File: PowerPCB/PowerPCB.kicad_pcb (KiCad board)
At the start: 2 copper layers, 140 x 70 mm, 60 parts, among them J1 Conn_01x03_Male, J2 Conn_01x10_Male, J3 Conn_01x07_Male, K1 1721081-5, K2 1721081-5, K3 1721081-5, Q1 Q_PMOS_DGS, U1 NCP1117-5.0_SOT223, U2 NCP1117-3.3_SOT223, U3 MCP2562-E-P, U4 MCP2562-E-P, U5 STM32F413ZHTx

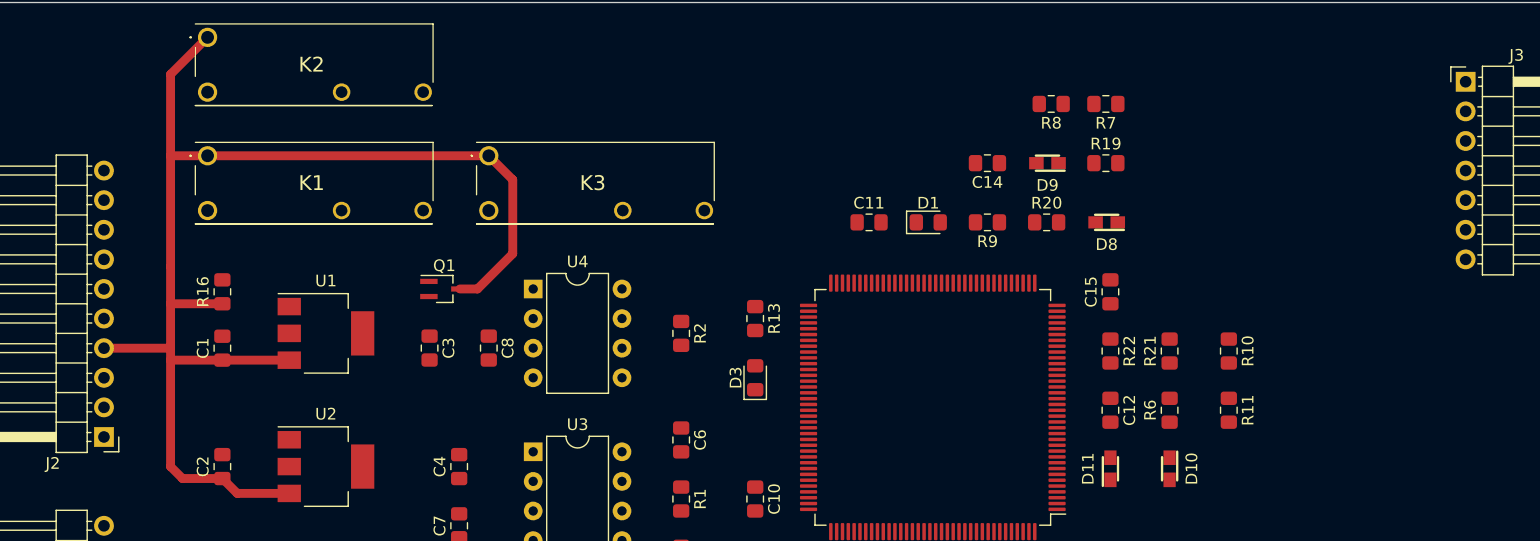
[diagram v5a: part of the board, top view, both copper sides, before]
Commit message: Routed most of Fan circuitry
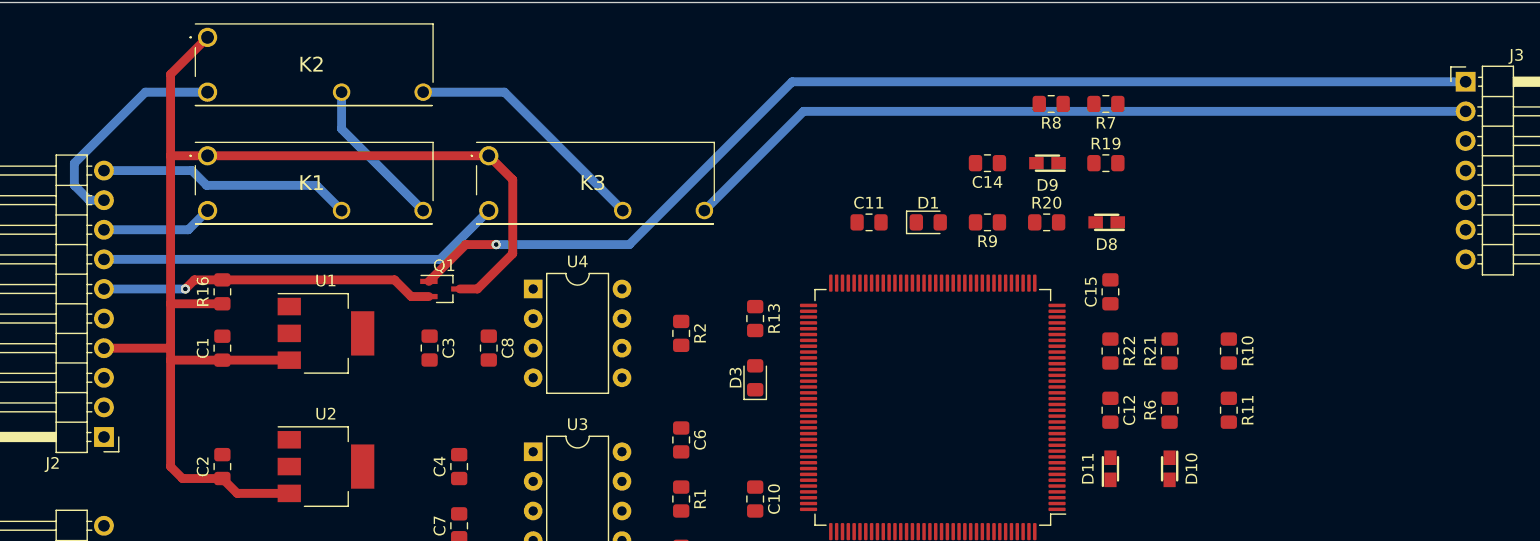
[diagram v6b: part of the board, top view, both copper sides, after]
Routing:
- net /Fan/Fan+: track 0.00 -> 96.1 mm, vias 0 -> 1
- net /Fan/Fan-: track 0.00 -> 68.8 mm
- net /Fan/FanCtrl: track 0.00 -> 34.8 mm
- net /Fan/FanPWM: track 0.00 -> 28.8 mm, vias 0 -> 1
- net Net-(J2-Pad10): track 0.00 -> 21.8 mm
- net GND: track 0.00 -> 21.3 mm
- net Net-(J2-Pad9): track 0.00 -> 18.9 mm
- net Net-(K1-Pad4): track 0.00 -> 13.1 mm
- net Net-(J2-Pad8): track 0.00 -> 9.57 mm
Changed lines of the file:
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@@
     (thickness 1.6)
     (drawings 4)
-    (tracks 21)
+    (tracks 49)
     (zones 0)
     (modules 60)
@@
   (gr_line (start 43 114) (end 183 114) (layer Edge.Cuts) (width 0.05))
   (gr_line (start 43 44) (end 43 114) (layer Edge.Cuts) (width 0.05))
+  (segment (start 88.97 51.69) (end 82 51.69) (width 0.762) (layer B.Cu) (net 1))
+  (segment (start 99.13 61.85) (end 88.97 51.69) (width 0.762) (layer B.Cu) (net 1))
   (segment (start 70.505 74.685) (end 70.51 74.69) (width 0.762) (layer F.Cu) (net 2))
   (segment (start 64.77 74.685) (end 70.505 74.685) (width 0.762) (layer F.Cu) (net 2))
@@
   (segment (start 60.325 50.165) (end 63.5 46.99) (width 0.762) (layer F.Cu) (net 2))
   (segment (start 63.5 57.15) (end 60.325 57.15) (width 0.762) (layer F.Cu) (net 2))
-  (segment (start 60.325 66.675) (end 60.325 57.15) (width 0.762) (layer F.Cu) (net 2))
-  (segment (start 60.325 57.15) (end 60.325 50.165) (width 0.762) (layer F.Cu) (net 2))
   (segment (start 60.325 69.85) (end 64.77 69.85) (width 0.762) (layer F.Cu) (net 2))
-  (segment (start 60.325 69.85) (end 60.325 66.675) (width 0.762) (layer F.Cu) (net 2))
   (segment (start 61.35 84.845) (end 64.77 84.845) (width 0.762) (layer F.Cu) (net 2))
   (segment (start 60.325 83.82) (end 61.35 84.845) (width 0.762) (layer F.Cu) (net 2))
   (segment (start 54.61 73.66) (end 60.325 73.66) (width 0.762) (layer F.Cu) (net 2))
-  (segment (start 60.325 69.85) (end 60.325 73.66) (width 0.762) (layer F.Cu) (net 2))
-  (segment (start 60.325 73.66) (end 60.325 83.82) (width 0.762) (layer F.Cu) (net 2))
   (segment (start 64.77 74.685) (end 60.325 74.685) (width 0.762) (layer F.Cu) (net 2))
   (segment (start 63.5 57.15) (end 87.63 57.15) (width 0.762) (layer F.Cu) (net 2))
@@
   (segment (start 89.686 59.206) (end 87.63 57.15) (width 0.762) (layer F.Cu) (net 2))
   (segment (start 89.686 65.556) (end 89.686 59.206) (width 0.762) (layer F.Cu) (net 2))
+  (segment (start 60.325 83.82) (end 60.325 50.165) (width 0.762) (layer F.Cu) (net 2))
+  (segment (start 61.85 63.5) (end 63.5 61.85) (width 0.762) (layer B.Cu) (net 7))
+  (segment (start 54.61 63.5) (end 61.85 63.5) (width 0.762) (layer B.Cu) (net 7))
+  (segment (start 83.44 66.04) (end 87.63 61.85) (width 0.762) (layer B.Cu) (net 8))
+  (segment (start 54.61 66.04) (end 83.44 66.04) (width 0.762) (layer B.Cu) (net 8))
+  (segment (start 54.61 68.58) (end 61.595 68.58) (width 0.762) (layer B.Cu) (net 9))
+  (via (at 61.595 68.58) (size 0.8) (drill 0.4) (layers F.Cu B.Cu) (net 9))
+  (segment (start 64.77 67.8) (end 62.375 67.8) (width 0.762) (layer F.Cu) (net 9))
+  (segment (start 62.375 67.8) (end 61.595 68.58) (width 0.762) (layer F.Cu) (net 9))
+  (segment (start 80.978 69.23) (end 82.49 69.23) (width 0.762) (layer F.Cu) (net 9))
+  (segment (start 79.548 67.8) (end 80.978 69.23) (width 0.762) (layer F.Cu) (net 9))
+  (segment (start 64.77 67.8) (end 79.548 67.8) (width 0.762) (layer F.Cu) (net 9))
+  (segment (start 114.64 53.34) (end 171.45 53.34) (width 0.762) (layer B.Cu) (net 10))
+  (segment (start 106.13 61.85) (end 114.64 53.34) (width 0.762) (layer B.Cu) (net 10))
+  (via (at 88.265 64.77) (size 0.8) (drill 0.4) (layers F.Cu B.Cu) (net 11))
+  (segment (start 82.49 67.93) (end 85.65 64.77) (width 0.762) (layer F.Cu) (net 11))
+  (segment (start 85.65 64.77) (end 88.265 64.77) (width 0.762) (layer F.Cu) (net 11))
+  (segment (start 88.265 64.77) (end 99.695 64.77) (width 0.762) (layer B.Cu) (net 11))
+  (segment (start 113.665 50.8) (end 171.45 50.8) (width 0.762) (layer B.Cu) (net 11))
+  (segment (start 99.695 64.77) (end 113.665 50.8) (width 0.762) (layer B.Cu) (net 11))
+  (segment (start 75 61.85) (end 72.84 59.69) (width 0.762) (layer B.Cu) (net 16))
+  (segment (start 63.420882 59.69) (end 62.150882 58.42) (width 0.762) (layer B.Cu) (net 16))
+  (segment (start 72.84 59.69) (end 63.420882 59.69) (width 0.762) (layer B.Cu) (net 16))
+  (segment (start 54.61 58.42) (end 62.150882 58.42) (width 0.762) (layer B.Cu) (net 16))
+  (segment (start 58.165 51.69) (end 63.5 51.69) (width 0.762) (layer B.Cu) (net 17))
+  (segment (start 52.07 59.69) (end 52.07 57.785) (width 0.762) (layer B.Cu) (net 17))
+  (segment (start 54.61 60.96) (end 53.34 60.96) (width 0.762) (layer B.Cu) (net 17))
+  (segment (start 52.07 57.785) (end 58.165 51.69) (width 0.762) (layer B.Cu) (net 17))
+  (segment (start 53.34 60.96) (end 52.07 59.69) (width 0.762) (layer B.Cu) (net 17))
+  (segment (start 75 54.85) (end 82 61.85) (width 0.762) (layer B.Cu) (net 20))
+  (segment (start 75 51.69) (end 75 54.85) (width 0.762) (layer B.Cu) (net 20))
 )

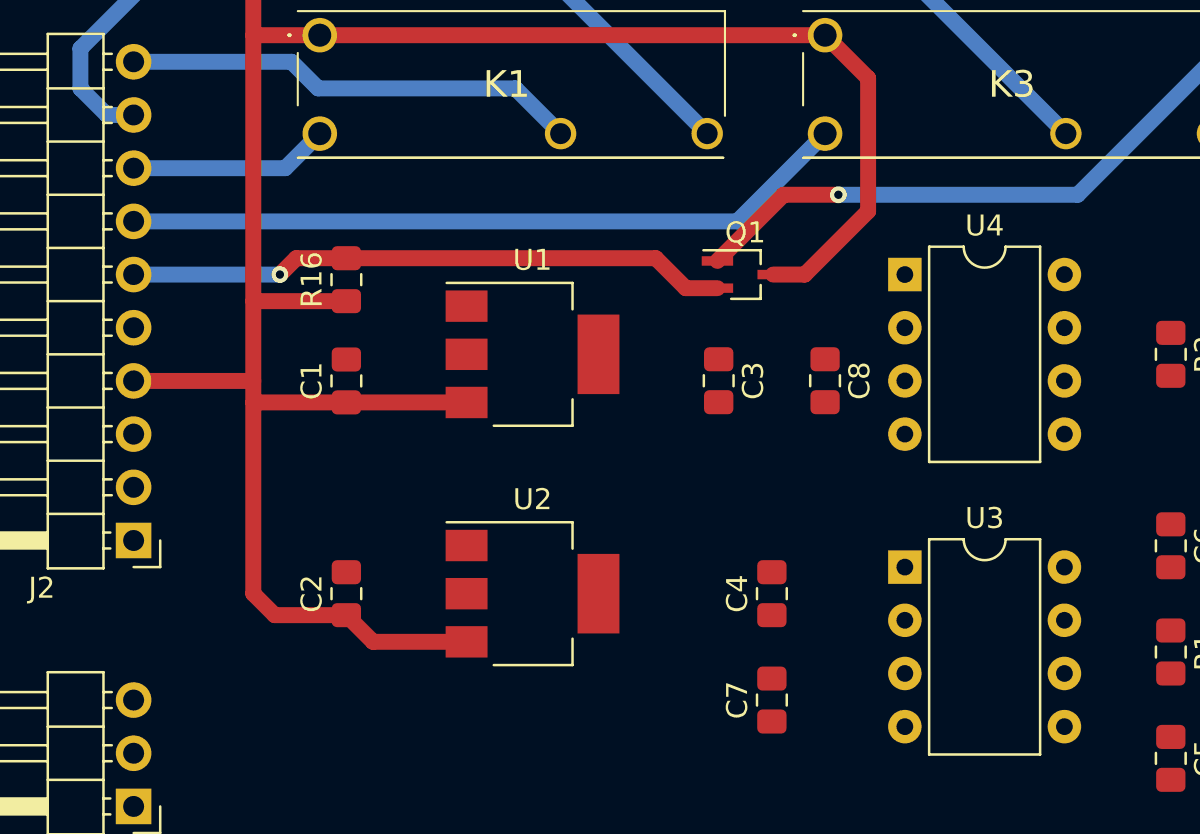
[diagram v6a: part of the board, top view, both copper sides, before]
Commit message: Routed 30 mils GND traces
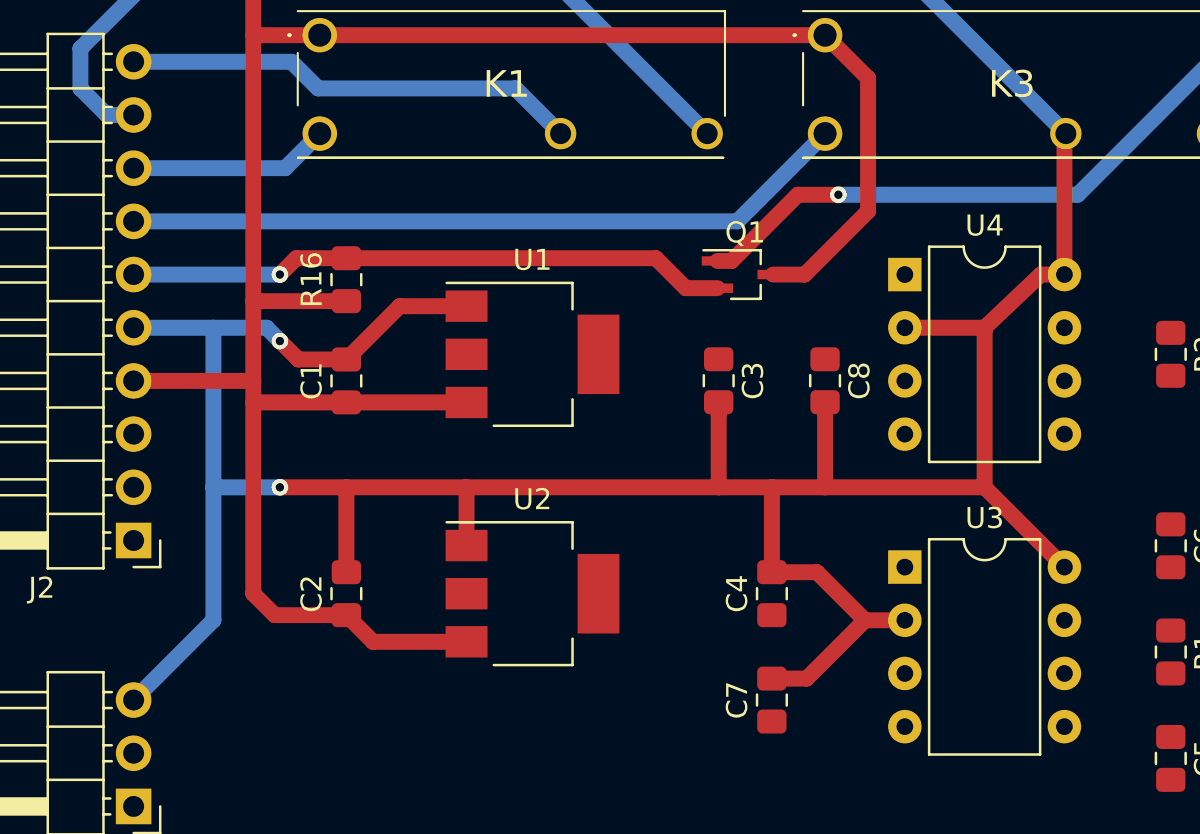
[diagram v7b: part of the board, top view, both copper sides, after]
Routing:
- net GND: track 21.3 -> 155.4 mm, vias 0 -> 2
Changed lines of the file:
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@@
     (thickness 1.6)
     (drawings 4)
-    (tracks 49)
+    (tracks 89)
     (zones 0)
     (modules 60)
@@
   (segment (start 88.97 51.69) (end 82 51.69) (width 0.762) (layer B.Cu) (net 1))
   (segment (start 99.13 61.85) (end 88.97 51.69) (width 0.762) (layer B.Cu) (net 1))
+  (segment (start 54.61 71.12) (end 58.42 71.12) (width 0.762) (layer B.Cu) (net 1))
+  (segment (start 58.42 71.12) (end 58.42 78.74) (width 0.762) (layer B.Cu) (net 1))
+  (via (at 61.595 78.74) (size 0.8) (drill 0.4) (layers F.Cu B.Cu) (net 1))
+  (segment (start 58.42 78.74) (end 61.595 78.74) (width 0.762) (layer B.Cu) (net 1))
+  (segment (start 95.25 78.74) (end 99.06 82.55) (width 0.762) (layer F.Cu) (net 1))
+  (segment (start 64.77 82.795) (end 64.77 78.74) (width 0.762) (layer F.Cu) (net 1))
+  (segment (start 61.595 78.74) (end 64.77 78.74) (width 0.762) (layer F.Cu) (net 1))
+  (segment (start 70.51 81.52) (end 70.51 78.765) (width 0.762) (layer F.Cu) (net 1))
+  (segment (start 70.51 78.765) (end 70.485 78.74) (width 0.762) (layer F.Cu) (net 1))
+  (segment (start 64.77 78.74) (end 70.485 78.74) (width 0.762) (layer F.Cu) (net 1))
+  (via (at 61.595 71.755) (size 0.8) (drill 0.4) (layers F.Cu B.Cu) (net 1))
+  (segment (start 64.77 72.635) (end 62.475 72.635) (width 0.762) (layer F.Cu) (net 1))
+  (segment (start 62.475 72.635) (end 61.595 71.755) (width 0.762) (layer F.Cu) (net 1))
+  (segment (start 60.96 71.12) (end 58.42 71.12) (width 0.762) (layer B.Cu) (net 1))
+  (segment (start 61.595 71.755) (end 60.96 71.12) (width 0.762) (layer B.Cu) (net 1))
+  (segment (start 67.315 70.09) (end 70.51 70.09) (width 0.762) (layer F.Cu) (net 1))
+  (segment (start 64.77 72.635) (end 67.315 70.09) (width 0.762) (layer F.Cu) (net 1))
+  (segment (start 82.55 75.251) (end 82.55 78.74) (width 0.762) (layer F.Cu) (net 1))
+  (segment (start 82.55 74.676) (end 82.55 75.251) (width 0.762) (layer F.Cu) (net 1))
+  (segment (start 70.485 78.74) (end 82.55 78.74) (width 0.762) (layer F.Cu) (net 1))
+  (segment (start 87.63 74.676) (end 87.63 78.74) (width 0.762) (layer F.Cu) (net 1))
+  (segment (start 87.63 78.74) (end 95.25 78.74) (width 0.762) (layer F.Cu) (net 1))
+  (segment (start 95.25 71.25863) (end 95.25 78.74) (width 0.762) (layer F.Cu) (net 1))
+  (segment (start 99.06 68.58) (end 97.92863 68.58) (width 0.762) (layer F.Cu) (net 1))
+  (segment (start 91.44 71.12) (end 95.25 71.12) (width 0.762) (layer F.Cu) (net 1))
+  (segment (start 97.92863 68.58) (end 95.25 71.12) (width 0.762) (layer F.Cu) (net 1))
+  (segment (start 95.25 71.12) (end 95.25 71.25863) (width 0.762) (layer F.Cu) (net 1))
+  (segment (start 85.09 82.795) (end 85.09 78.74) (width 0.762) (layer F.Cu) (net 1))
+  (segment (start 82.55 78.74) (end 85.09 78.74) (width 0.762) (layer F.Cu) (net 1))
+  (segment (start 85.09 78.74) (end 87.63 78.74) (width 0.762) (layer F.Cu) (net 1))
+  (segment (start 85.09 82.795) (end 87.24 82.795) (width 0.762) (layer F.Cu) (net 1))
+  (segment (start 89.535 85.09) (end 91.44 85.09) (width 0.762) (layer F.Cu) (net 1))
+  (segment (start 87.24 82.795) (end 89.535 85.09) (width 0.762) (layer F.Cu) (net 1))
+  (segment (start 58.42 85.09) (end 54.61 88.9) (width 0.762) (layer B.Cu) (net 1))
+  (segment (start 58.42 78.74) (end 58.42 85.09) (width 0.762) (layer B.Cu) (net 1))
+  (segment (start 86.75 87.875) (end 85.09 87.875) (width 0.762) (layer F.Cu) (net 1))
+  (segment (start 89.535 85.09) (end 86.75 87.875) (width 0.762) (layer F.Cu) (net 1))
+  (segment (start 99.06 61.92) (end 99.13 61.85) (width 0.762) (layer F.Cu) (net 1))
+  (segment (start 99.06 68.58) (end 99.06 61.92) (width 0.762) (layer F.Cu) (net 1))
   (segment (start 70.505 74.685) (end 70.51 74.69) (width 0.762) (layer F.Cu) (net 2))
   (segment (start 64.77 74.685) (end 70.505 74.685) (width 0.762) (layer F.Cu) (net 2))
@@
   (segment (start 106.13 61.85) (end 114.64 53.34) (width 0.762) (layer B.Cu) (net 10))
   (via (at 88.265 64.77) (size 0.8) (drill 0.4) (layers F.Cu B.Cu) (net 11))
-  (segment (start 82.49 67.93) (end 85.65 64.77) (width 0.762) (layer F.Cu) (net 11))
-  (segment (start 85.65 64.77) (end 88.265 64.77) (width 0.762) (layer F.Cu) (net 11))
   (segment (start 88.265 64.77) (end 99.695 64.77) (width 0.762) (layer B.Cu) (net 11))
   (segment (start 113.665 50.8) (end 171.45 50.8) (width 0.762) (layer B.Cu) (net 11))
   (segment (start 99.695 64.77) (end 113.665 50.8) (width 0.762) (layer B.Cu) (net 11))
+  (segment (start 82.49 67.93) (end 83.17 67.93) (width 0.762) (layer F.Cu) (net 11))
+  (segment (start 86.33 64.77) (end 88.265 64.77) (width 0.762) (layer F.Cu) (net 11))
+  (segment (start 83.17 67.93) (end 86.33 64.77) (width 0.762) (layer F.Cu) (net 11))
   (segment (start 75 61.85) (end 72.84 59.69) (width 0.762) (layer B.Cu) (net 16))
   (segment (start 63.420882 59.69) (end 62.150882 58.42) (width 0.762) (layer B.Cu) (net 16))
